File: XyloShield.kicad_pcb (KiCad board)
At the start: 2 copper layers, 19 parts, among them J1 XLR3, J2 XLR3, J3 Conn_01x02, J4 Conn_01x02, J5 Conn_01x02, J6 Conn_Coaxial, J7 Conn_01x02, U1 4050, U2 MAX485E, U3 RFM26W

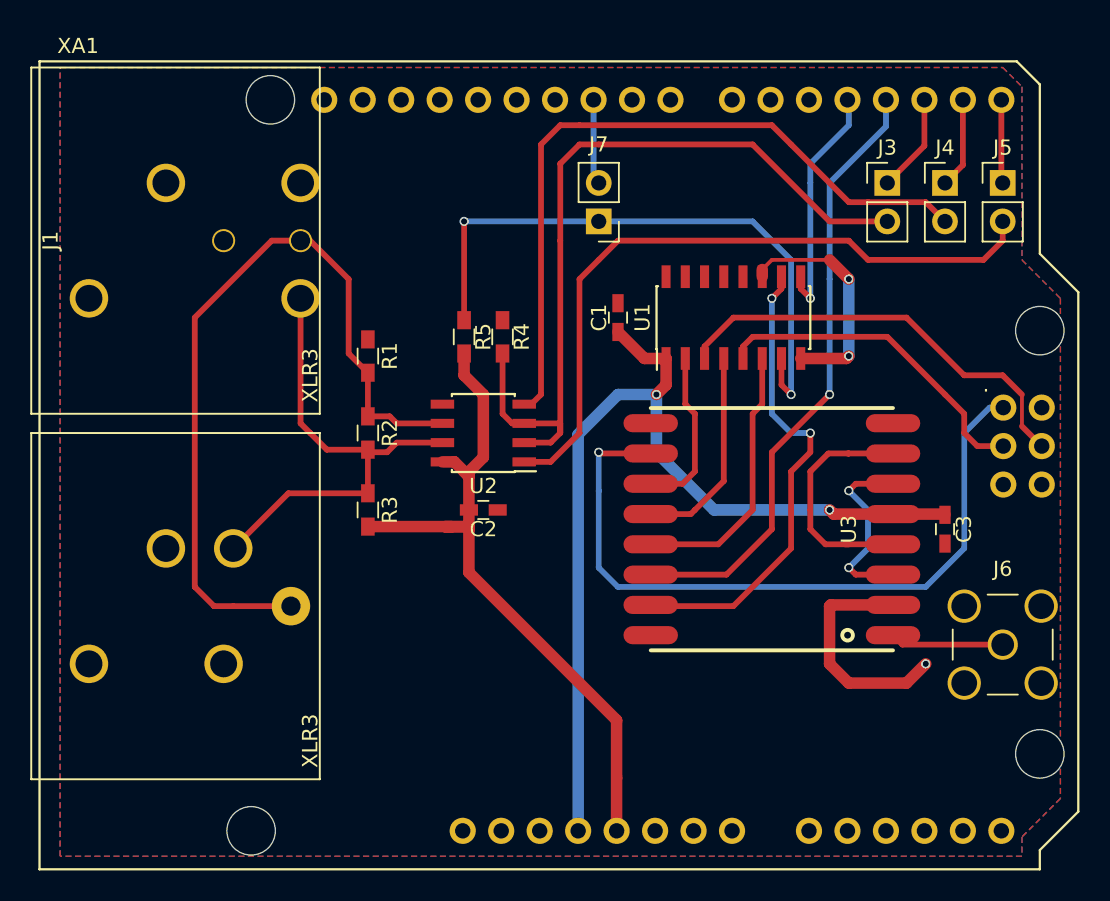
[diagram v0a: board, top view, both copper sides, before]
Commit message: Some cleanup (adjusted track widths, used finer grid for component placement)
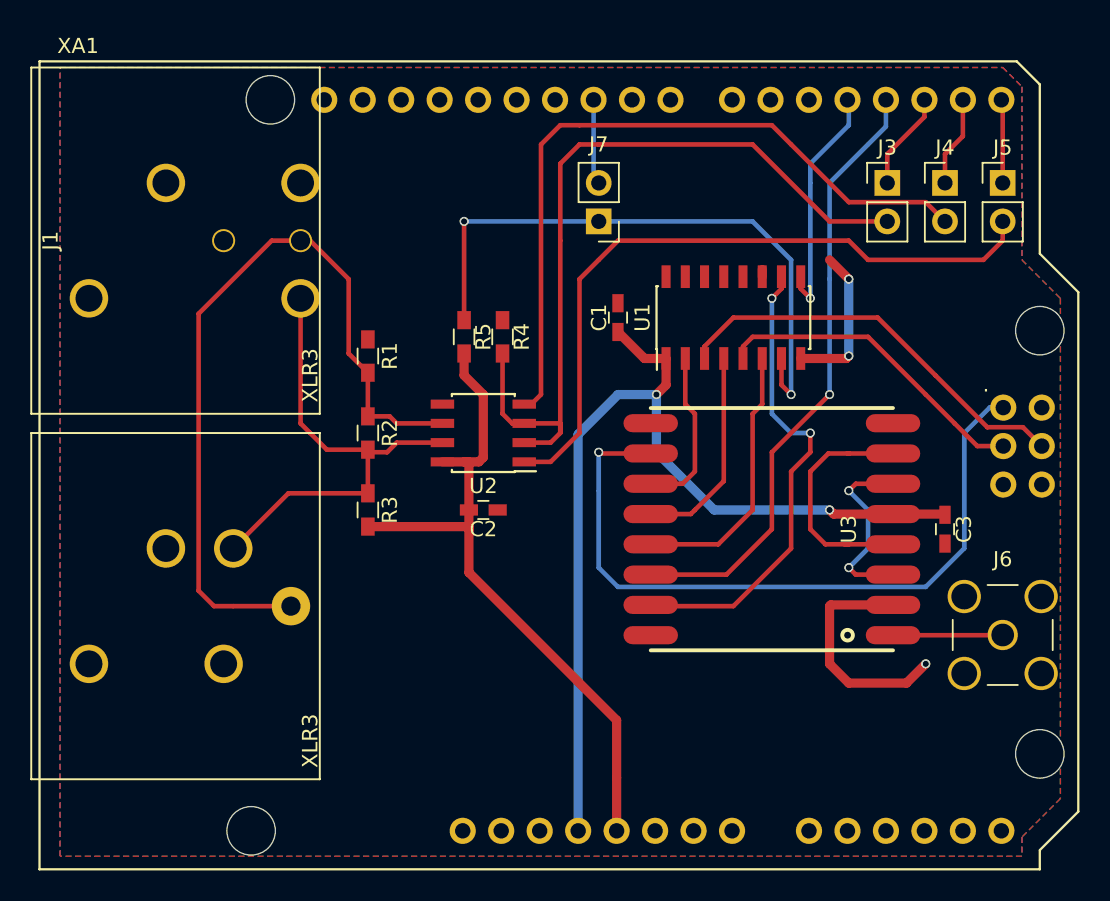
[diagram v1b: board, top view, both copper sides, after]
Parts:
- moved J6 0.64 mm to (212.1, 89.5)
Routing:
- net GND: track 30.7 -> 26.0 mm
- net +5V: track 47.2 -> 45.8 mm
- net Net-(U1-Pad3): track 28.6 -> 27.4 mm
- net Net-(U1-Pad5): track 22.0 -> 21.2 mm
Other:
- net class Default: trace_width 0.381 -> 0.3048
- net class Power: trace_width 0.762 -> 0.6096

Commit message: - Fixed orientation of J7 - Added some more silkscreen text - Exported Gerbers
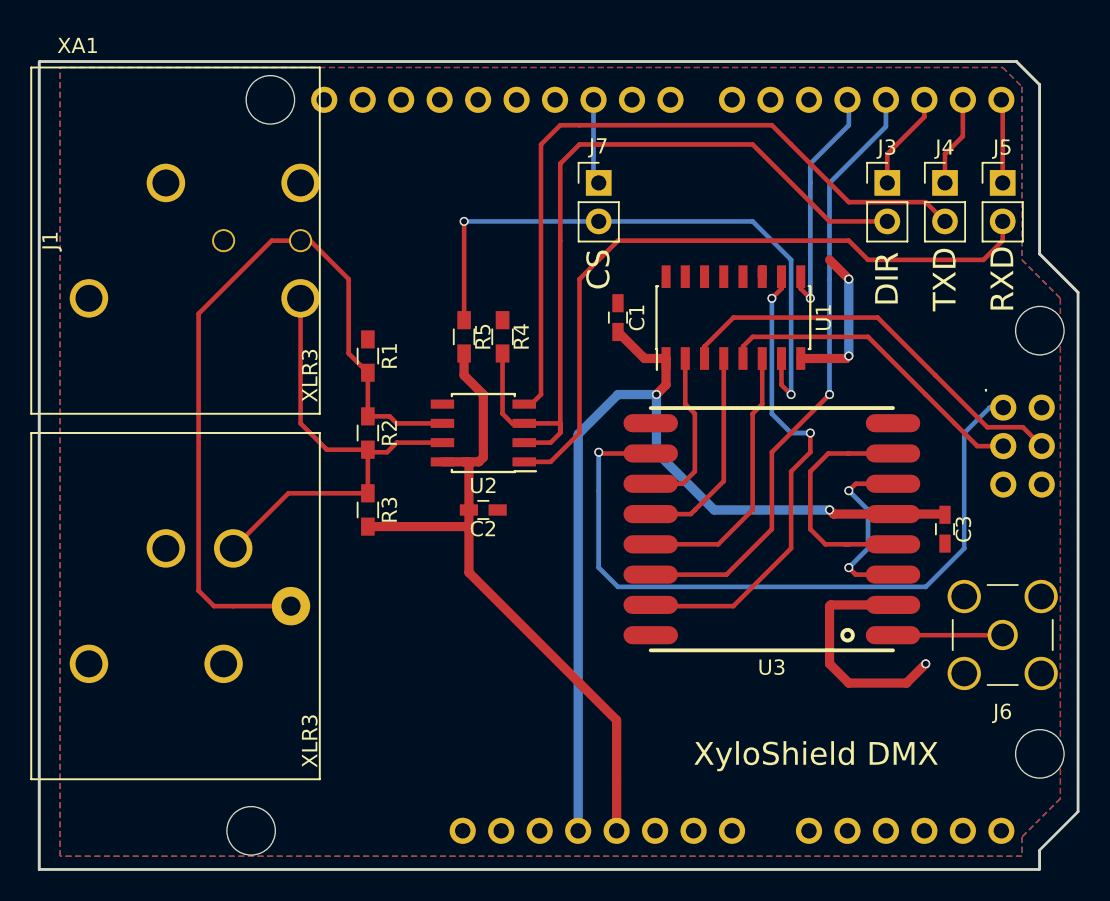
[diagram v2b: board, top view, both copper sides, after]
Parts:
- moved J7 2.54 mm to (185.4, 59.7), turned to 0 degrees
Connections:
- R5 pad 1: Net-(J7-Pad1) -> Net-(J7-Pad2)
- U1 pad 7: Net-(J7-Pad1) -> Net-(J7-Pad2)
- XA1 pad D10: Net-(J7-Pad2) -> Net-(J7-Pad1)
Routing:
- net Net-(J7-Pad2): track 5.63 -> 40.7 mm, vias 0 -> 2
- net Net-(J7-Pad1): track 40.7 -> 5.63 mm, vias 2 -> 0
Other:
- board outline added: 68.6 x 53.3 mm
- board text added: "CS"
- board text added: "DIR"
- board text added: "RXD"
- board text added: "TXD"
- board text added: "XyloShield DMX"
